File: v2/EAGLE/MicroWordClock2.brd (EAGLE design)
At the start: 20.3 x 20.3 mm, 20 parts, among them IC1 ATMEGA328P, IC2 DS1307SMD

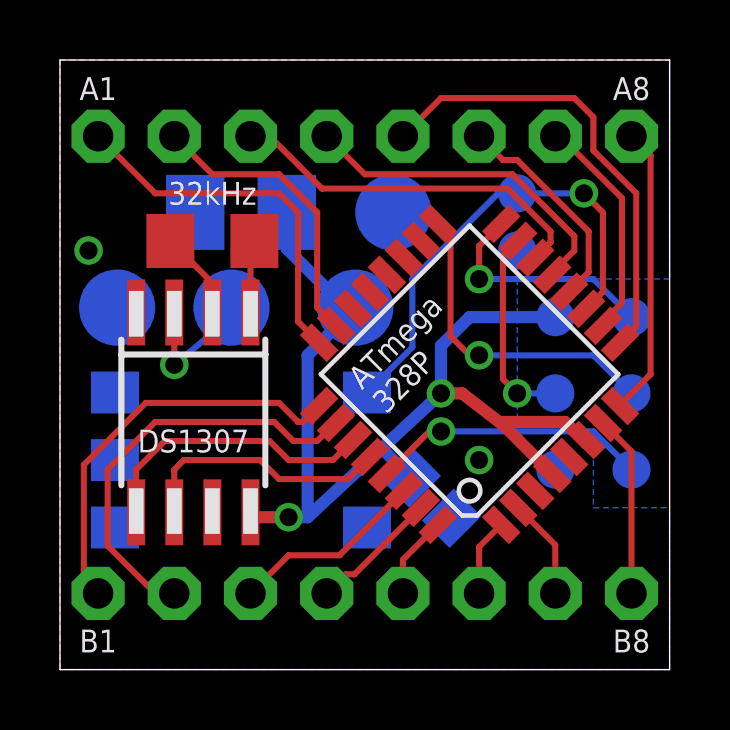
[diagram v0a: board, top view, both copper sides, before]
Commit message: Changed schematic to free up serial port Widened all tracks to 12mil Panelised to put 9 onto a 5x5 "panel".
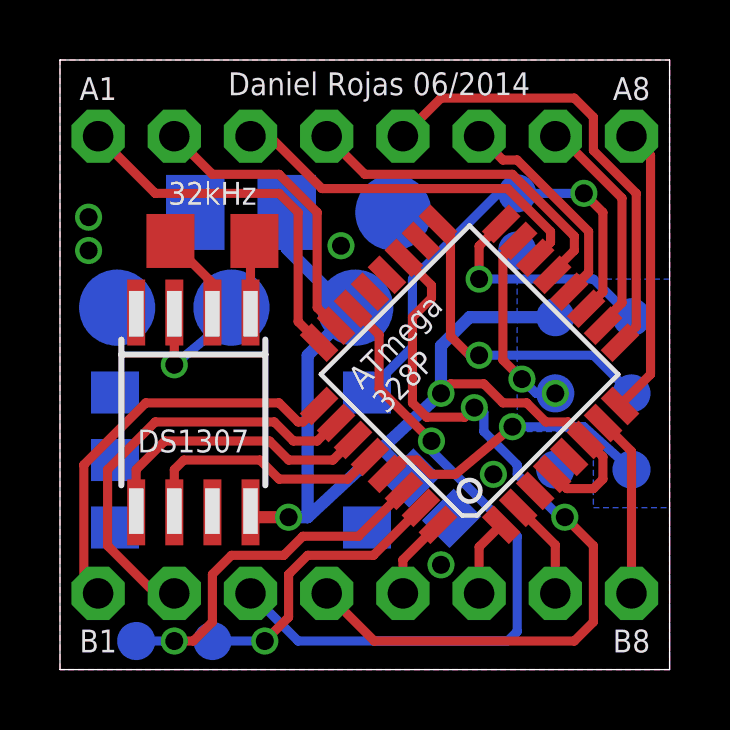
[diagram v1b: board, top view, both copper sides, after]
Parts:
- added R, T: TPB1,27, testpad:B1,27
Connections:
- new net N$1: IC1.31, T.TP
- new net N$3: IC1.30, R.TP
- net B3: now also IC1.22; no longer IC1.30
- net B4: now also IC1.19; no longer IC1.31
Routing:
- net B4: track 4.32 -> 26.7 mm, vias 0 -> 2
- net B3: track 6.53 -> 22.7 mm, vias 0 -> 1
- net N$3: track 0.00 -> 11.9 mm, vias 0 -> 1
- net N$1: track 0.00 -> 9.63 mm, vias 0 -> 1
- net +5V: track 37.0 -> 38.3 mm
- net MOSI: track 6.76 -> 6.39 mm, vias 1 -> 2
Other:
- board text added: "MicroWordClock v2.1"
- board text removed: "MicroWordClock v2"
